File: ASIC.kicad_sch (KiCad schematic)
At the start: 67 parts, among them U10 BM1370_mode0, U11 MCP1824T-1202E/OT, U12 MCP1824T-0802E, U7 SN74AVC4T774, U8 25MHz, U9 BM1370_mode0

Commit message: more parts placement
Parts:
- removed U10, U9: BM1370_mode0, bitaxe:BM1370, symbol bitaxe:BM1370_mode0
- added U10, U9: BM1370_mode1, bitaxe:BM1370, symbol bitaxe:BM1370_mode1
- TP7: value RO -> RI
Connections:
- net 0V8: now also U10.14 (VDDIO_08_0), U9.17 (VDDIO_08_1)
- net 0V8_1: now also U9.14 (VDDIO_08_0)
- net 0V8_2: now also U10.17 (VDDIO_08_1)
- net 1V2: now also U10.15 (VDDIO_12_0), U9.16 (VDDIO_12_1)
- net 1V2_1: now also U9.15 (VDDIO_12_0)
- net 1V2_2: now also U10.16 (VDDIO_12_1)
- net BI: now also R24.2, U9.9 (BI); no longer R24.1
- net CLKI: now also U9.8 (CLKI)
- net GND: now also R24.1, U10.13 (PLL_VSS), U10.18 (VSS), U10.27 (VSS), U10.32 (VSS), U10.4 (VSS), U9.13 (PLL_VSS), U9.18 (VSS), U9.27 (VSS), U9.32 (VSS), U9.4 (VSS); no longer R24.2
- net RST_1V2: now also U9.5 (NRSTI); no longer R25.2
- net RX_1V2: now also U9.7 (RO)
- net TEMP1_N: now also U9.21 (TEMP_N)
- net TEMP1_P: now also U9.20 (TEMP_P)
- net TEMP2_N: now also U10.21 (TEMP_N)
- net TEMP2_P: now also U10.20 (TEMP_P)
- net TX_1V2: now also U9.6 (CI)
- net Vcore: now also U10.31 (VDD), U9.31 (VDD)
- net at TP10.1: now also U9.10 (ROSC_SEL)
- net at R26.2, TP12.1: now also U9.11 (LITE_PAD)
- net at C70.2, C71.1, C72.2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: now also U10.3 (VDD1_0), U9.28 (VDD1_1)
- net at C69.2, C70.1, C73.2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: now also U10.2 (VDD2_0), U9.29 (VDD2_1)
- net at C78.2, C79.1: now also U10.28 (VDD1_1)
- net at TP5.1: now also U10.22 (BO)
- net at C68.2, C69.1, C74.2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: now also U10.1 (VDD3_0), U9.30 (VDD3_1)
- net at TP6.1: now also U10.23 (CLKO)
- net at C64.2, C65.1: now also U9.3 (VDD1_0)
- net at C65.2, C66.1: now also U9.2 (VDD2_0)
- net at R28.2, TP13.1: now also U10.11 (LITE_PAD)
- net at TP8.1: now also U10.25 (CO)
- net at C76.2, C77.1: now also U10.30 (VDD3_1)
- net at TP7.1: now also U10.24 (RI)
- net at TP11.1: now also U10.10 (ROSC_SEL)
- net at C66.2, C67.1: now also U9.1 (VDD3_0)
- net at R27.2: now also U10.9 (BI), U9.22 (BO)
- net at TP14.1: now also U9.12 (INV_CLKO)
- net at TP9.1: now also U10.26 (NRSTO)
- net at C77.2, C78.1: now also U10.29 (VDD2_1)
- net at TP16.1: now also U10.12 (INV_CLKO)
- new net: U10.8 (CLKI), U9.23 (CLKO)
- new net: U10.7 (RO), U9.24 (RI)
- new net: U10.6 (CI), U9.25 (CO)
- new net: U10.5 (NRSTI), U9.26 (NRSTO)
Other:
- moved on the sheet: R24, TP5, TP6, TP7, TP8, TP9

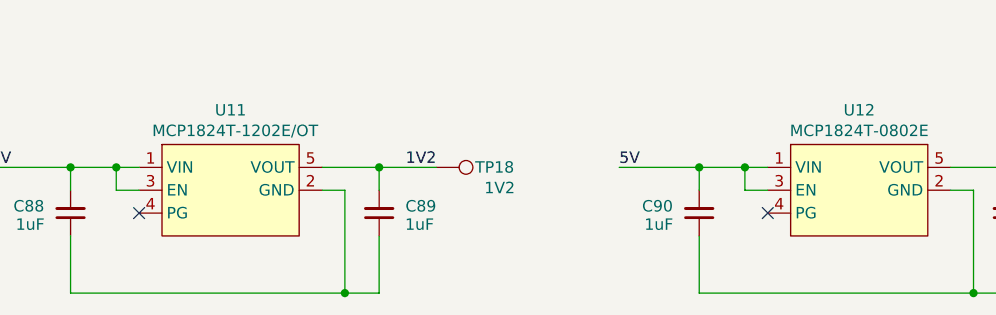
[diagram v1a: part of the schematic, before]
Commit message: More parts placement
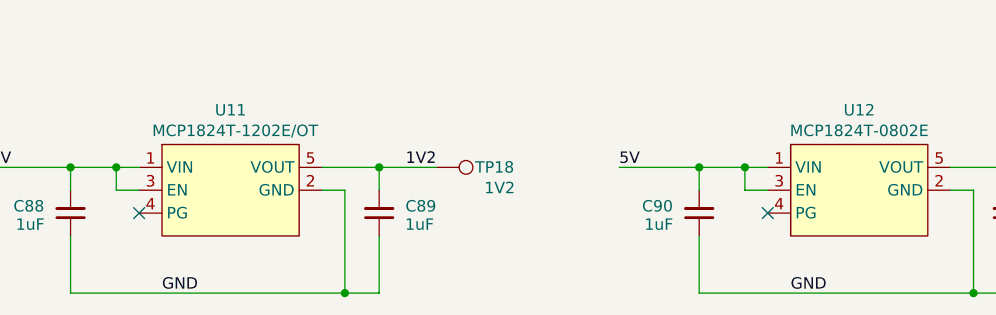
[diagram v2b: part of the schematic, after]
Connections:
- net GND: now also C88.1, C89.1, C90.1, C91.1, U11.2 (GND), U12.2 (GND)
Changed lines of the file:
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@@
+		)
+	)
+	(label "GND"
+		(at 119.38 187.96 0)
+		(fields_autoplaced yes)
+		(effects
+			(font
+				(size 1.27 1.27)
+			)
+			(justify left bottom)
 		)
 	)
@@
 		)
 	)
+	(label "GND"
+		(at 49.53 187.96 0)
+		(fields_autoplaced yes)
+		(effects
+			(font
+				(size 1.27 1.27)
+			)
+			(justify left bottom)
+		)
+	)

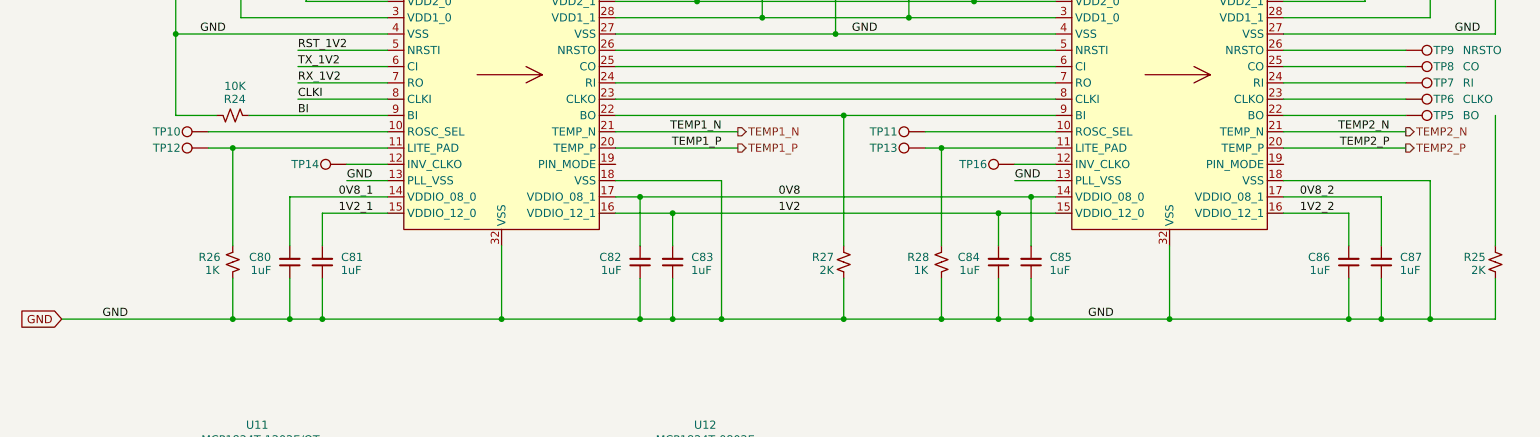
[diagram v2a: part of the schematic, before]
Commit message: Route main power paths
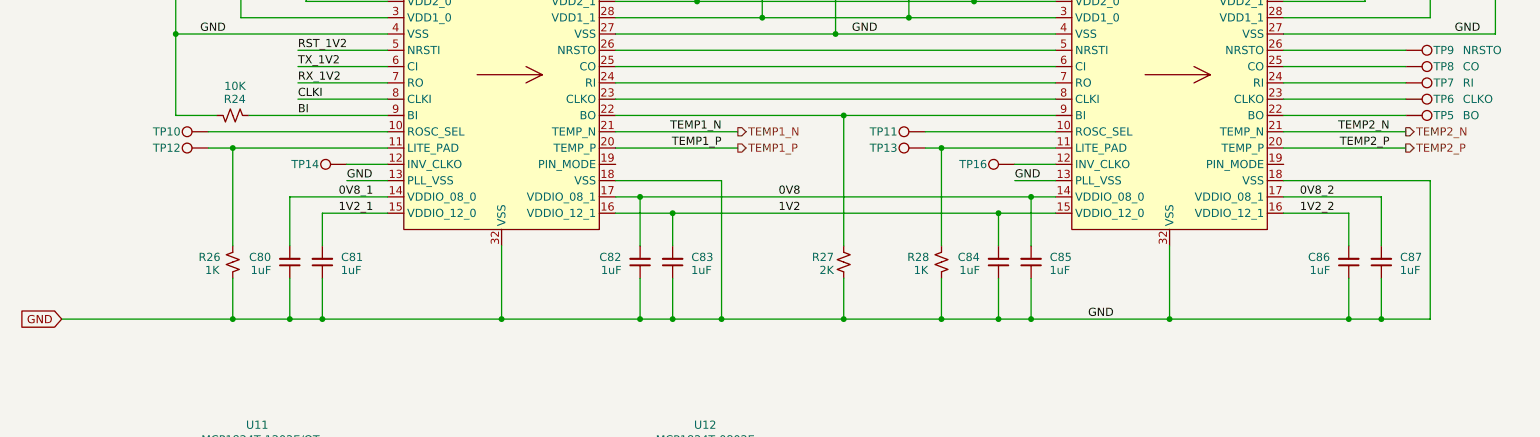
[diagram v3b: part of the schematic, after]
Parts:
- removed R25: 2K, Resistor_SMD:R_0402_1005Metric, symbol Device:R_Small_US
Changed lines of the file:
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@@
 	)
 	(junction
-		(at 240.03 151.13)
-		(diameter 0)
-		(color 0 0 0 0)
-	)
-	(junction
 		(at 219.71 87.63)
 		(diameter 0)
@@
 	(wire
 		(pts
-			(xy 250.19 151.13) (xy 250.19 144.78)
-		)
-		(stroke
-			(width 0)
-			(type default)
-		)
-	)
-	(wire
-		(pts
 			(xy 229.87 87.63) (xy 229.87 101.6)
 		)
@@
 	(wire
 		(pts
-			(xy 240.03 151.13) (xy 250.19 151.13)
-		)
-		(stroke
-			(width 0)
-			(type default)
-		)
-	)
-	(wire
-		(pts
 			(xy 185.42 50.8) (xy 181.61 50.8)
 		)
@@
 	(wire
 		(pts
-			(xy 250.19 119.38) (xy 250.19 139.7)
-		)
-		(stroke
-			(width 0)
-			(type default)
-		)
-	)
-	(wire
-		(pts
 			(xy 229.87 87.63) (xy 232.41 87.63)
 		)
@@
 		)
 	)
-	(label "GND"
-		(at 33.02 151.13 0)
-		(fields_autoplaced yes)
-		(effects
-			(font
-				(size 1.27 1.27)
-			)
-			(justify left bottom)
-		)
-	)
 	(label "TX_1V2"
 		(at 63.5 111.76 0)
@@
 					(unit 1)
 				)
-			)
-		)
-	)
-	(symbol
-		(lib_id "Device:R_Small_US")
-		(at 250.19 142.24 180)
-		(unit 1)
-		(exclude_from_sim no)
-		(in_bom yes)
-		(on_board yes)
-		(dnp no)
-		(property "Reference" "R25"
-			(at 248.666 141.478 0)
-			(effects
-				(font
-					(size 1.27 1.27)
-				)
-				(justify left)
-			)
-		)
-		(property "Value" "2K"
-			(at 248.666 143.51 0)
-			(effects
-				(font
-					(size 1.27 1.27)
-				)
-				(justify left)
-			)
-		)
-		(property "Footprint" "Resistor_SMD:R_0402_1005Metric"
-			(at 250.19 142.24 0)
-			(effects
-				(font
-					(size 1.27 1.27)
-				)
-				(hide yes)
-			)
-		)
-		(property "Datasheet" "~"
-			(at 250.19 142.24 0)
-			(effects
-				(font
-					(size 1.27 1.27)
-				)
-				(hide yes)
-			)
-		)
-		(property "Description" "Resistor, small US symbol"
-			(at 250.19 142.24 0)
-			(effects
-				(font
-					(size 1.27 1.27)
-				)
-				(hide yes)
-			)
-		)
-		(property "PARTNO" "RT0402BRD072KL"
-			(at 250.19 142.24 0)
-			(effects
-				(font
-					(size 1.27 1.27)
-				)
-				(hide yes)
-			)
-		)
-		(property "DK" "YAG2303CT-ND"
-			(at 250.19 142.24 0)
-			(effects
-				(font
-					(size 1.27 1.27)
-				)
-				(hide yes)
-			)
-		)
-		(pin "2"
-		)
-		(pin "1"
-		)
-		(instances
-			(project "BitaxeGT"
-				(path "/61fe8d2c-9301-4ad9-8caf-c47acfa835b0/5053a6d5-ae8d-4ae0-9f6e-0d65e80da719"
-					(reference "R25")
-					(unit 1)
-				)

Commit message: bypass cap size
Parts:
- C58, C63: footprint Capacitor_SMD:C_1210_3225Metric -> Capacitor_SMD:C_1206_3216Metric
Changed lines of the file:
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@@
 			)
 		)
-		(property "Footprint" "Capacitor_SMD:C_1210_3225Metric"
+		(property "Footprint" "Capacitor_SMD:C_1206_3216Metric"
 			(at 142.24 72.39 0)
 			(effects
@@
 			)
 		)
-		(property "Footprint" "Capacitor_SMD:C_1210_3225Metric"
+		(property "Footprint" "Capacitor_SMD:C_1206_3216Metric"
 			(at 246.38 72.39 0)
 			(effects

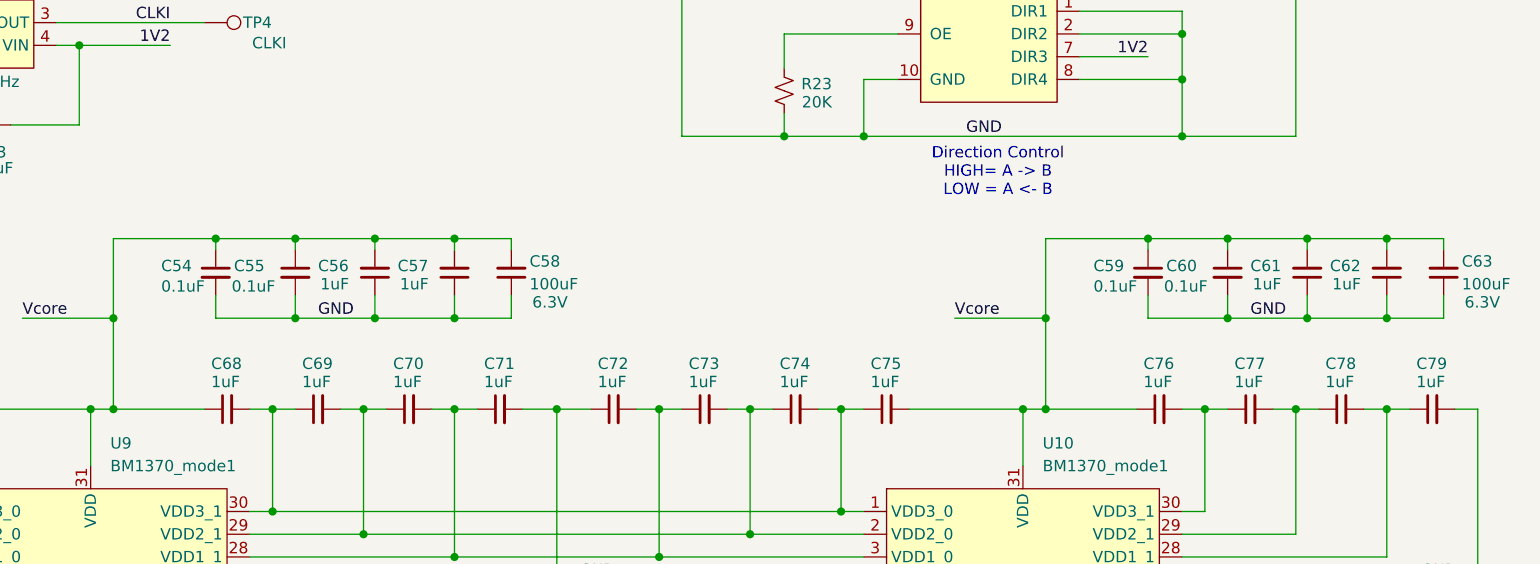
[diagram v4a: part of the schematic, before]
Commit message: change 10uf to 0402, change decouple caps to 5X10uf
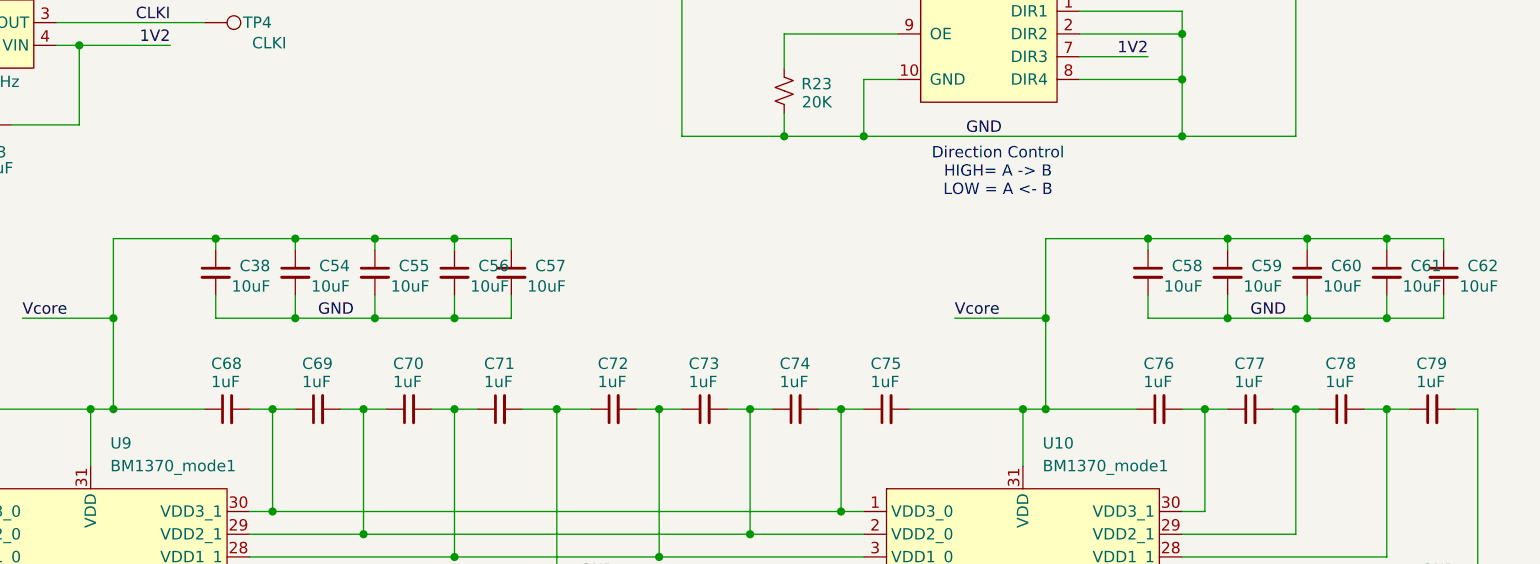
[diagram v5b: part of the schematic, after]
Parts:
- removed C63: 100uF, Capacitor_SMD:C_1206_3216Metric, symbol Device:C_Small
- added C38: 10uF, Capacitor_SMD:C_0402_1005Metric, symbol Device:C_Small
- C54, C55, C59, C60: value 0.1uF -> 10uF; DK 478-KGM05AR71C104KHCT-ND -> 490-5523-1-ND; PARTNO KGM05AR71C104KH -> GRM21BR61E106KA73L
- C56, C57, C61, C62: value 1uF -> 10uF; DK 587-5514-1-ND -> 490-5523-1-ND; PARTNO (none) -> GRM21BR61E106KA73L; PARTNUM EMK105BJ105MV-F -> (none)
- C58: value 100uF -> 10uF; footprint Capacitor_SMD:C_1206_3216Metric -> Capacitor_SMD:C_0402_1005Metric; DK 490-10534-1-ND -> 490-5523-1-ND; PARTNO GRM32EE70J107ME15L -> GRM21BR61E106KA73L; voltage 6.3V -> (none)
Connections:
- net GND: now also C56.2, C57.2, C58.2, C61.2, C62.2, C38.2; no longer C56.1, C57.1, C58.1, C61.1, C62.1
- net Vcore: now also C56.1, C57.1, C58.1, C61.1, C62.1, C38.1; no longer C56.2, C57.2, C58.2, C61.2, C62.2

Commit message: 10uf partnum
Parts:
- C38, C54, C55, C56, C57, C58, C59, C60, C61, C62: PARTNO GRM21BR61E106KA73L -> CL05A106MQ5NUNC
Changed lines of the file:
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@@
 			)
 		)
-		(property "PARTNO" "GRM21BR61E106KA73L"
+		(property "PARTNO" "CL05A106MQ5NUNC"
 			(at 231.14 72.39 0)
 			(effects
@@
 			)
 		)
-		(property "PARTNO" "GRM21BR61E106KA73L"
+		(property "PARTNO" "CL05A106MQ5NUNC"
 			(at 222.25 72.39 0)
 			(effects
@@
 			)
 		)
-		(property "PARTNO" "GRM21BR61E106KA73L"
+		(property "PARTNO" "CL05A106MQ5NUNC"
 			(at 240.03 72.39 0)
 			(effects
@@
 			)
 		)
-		(property "PARTNO" "GRM21BR61E106KA73L"
+		(property "PARTNO" "CL05A106MQ5NUNC"
 			(at 118.11 72.39 0)
 			(effects
@@
 			)
 		)
-		(property "PARTNO" "GRM21BR61E106KA73L"
+		(property "PARTNO" "CL05A106MQ5NUNC"
 			(at 142.24 72.39 0)
 			(effects
@@
 			)
 		)
-		(property "PARTNO" "GRM21BR61E106KA73L"
+		(property "PARTNO" "CL05A106MQ5NUNC"
 			(at 109.22 72.39 0)
 			(effects
@@
 			)
 		)
-		(property "PARTNO" "GRM21BR61E106KA73L"
+		(property "PARTNO" "CL05A106MQ5NUNC"
 			(at 213.36 72.39 0)
 			(effects
@@
 			)
 		)
-		(property "PARTNO" "GRM21BR61E106KA73L"
+		(property "PARTNO" "CL05A106MQ5NUNC"
 			(at 246.38 72.39 0)
 			(effects
@@
 			)
 		)
-		(property "PARTNO" "GRM21BR61E106KA73L"
+		(property "PARTNO" "CL05A106MQ5NUNC"
 			(at 127 72.39 0)
 			(effects
@@
 			)
 		)
-		(property "PARTNO" "GRM21BR61E106KA73L"
+		(property "PARTNO" "CL05A106MQ5NUNC"
 			(at 135.89 72.39 0)
 			(effects

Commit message: Changed 10uf caps to 0603
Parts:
- C38, C54, C55, C56, C57, C58, C59, C60, C61, C62: footprint Capacitor_SMD:C_0402_1005Metric -> Capacitor_SMD:C_0603_1608Metric; PARTNO CL05A106MQ5NUNC -> GRM188R61E106KA73D

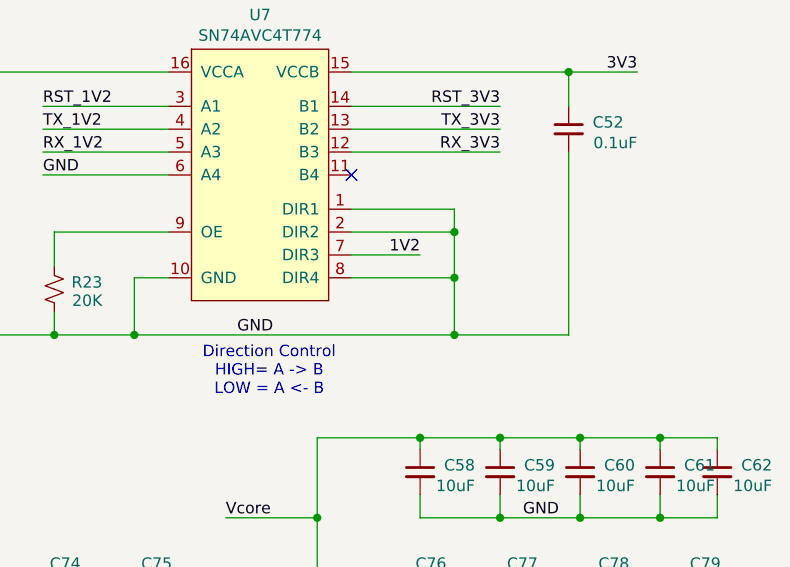
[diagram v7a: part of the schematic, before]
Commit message: fixed unused input on level shifter. Attached Vcore to ADC pin on the ESP32 for monitoring.
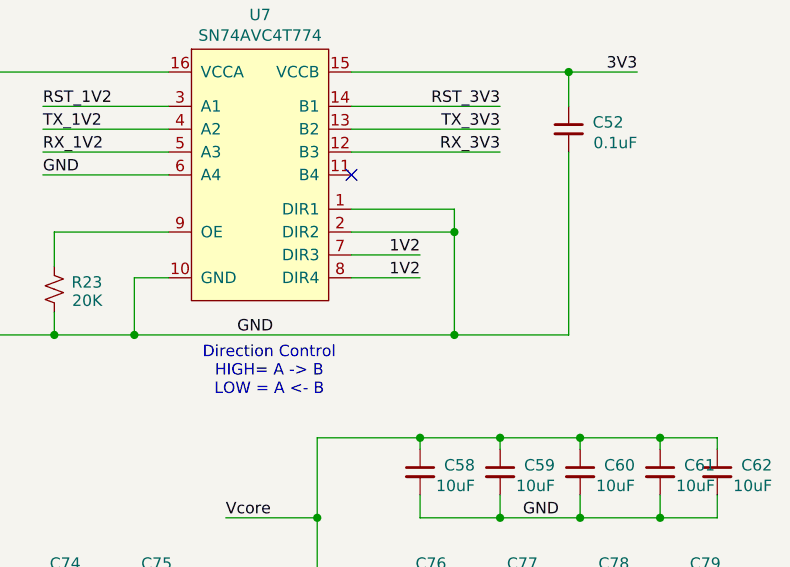
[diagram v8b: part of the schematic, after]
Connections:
- net 1V2: now also U7.8 (DIR4)
- net GND: no longer U7.8 (DIR4)
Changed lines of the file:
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@@
-	)
-	(junction
-		(at 217.17 50.8)
-		(diameter 0)
-		(color 0 0 0 0)
 	)
 	(junction
@@
 	(wire
 		(pts
-			(xy 217.17 45.72) (xy 217.17 50.8)
+			(xy 217.17 45.72) (xy 217.17 57.15)
 		)
 		(stroke
@@
 	(wire
 		(pts
+			(xy 205.74 50.8) (xy 213.36 50.8)
+		)
+		(stroke
+			(width 0)
+			(type default)
+		)
+	)
+	(wire
+		(pts
 			(xy 121.92 144.78) (xy 121.92 151.13)
 		)
@@
 	(wire
 		(pts
-			(xy 205.74 50.8) (xy 217.17 50.8)
-		)
-		(stroke
-			(width 0)
-			(type default)
-		)
-	)
-	(wire
-		(pts
 			(xy 135.89 104.14) (xy 158.75 104.14)
 		)
@@
 		(pts
 			(xy 172.72 134.62) (xy 172.72 139.7)
-		)
-		(stroke
-			(width 0)
-			(type default)
-		)
-	)
-	(wire
-		(pts
-			(xy 217.17 50.8) (xy 217.17 57.15)
 		)
 		(stroke
@@
 		(fields_autoplaced yes)
 		(effects
+			(font
+				(size 1.27 1.27)
+			)
+			(justify right bottom)
+		)
+	)
+	(label "1V2"
+		(at 213.36 50.8 180)
+		(fields_autoplaced yes)
+		(effects
